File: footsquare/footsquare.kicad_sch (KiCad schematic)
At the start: 6 parts, among them J1 USB_B, U1 Trill_Craft, U2 Teensy-LC

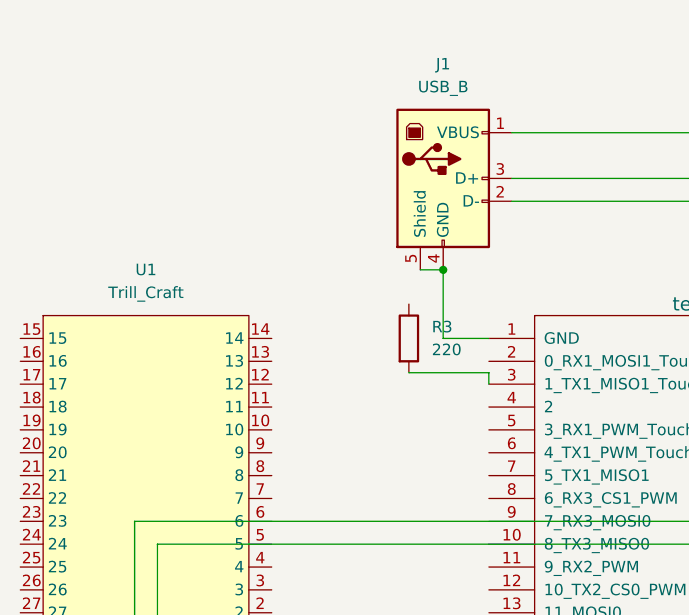
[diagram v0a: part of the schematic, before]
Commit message: new version with encoder and ground plane
-ground plane added
-encoder added
-outline added
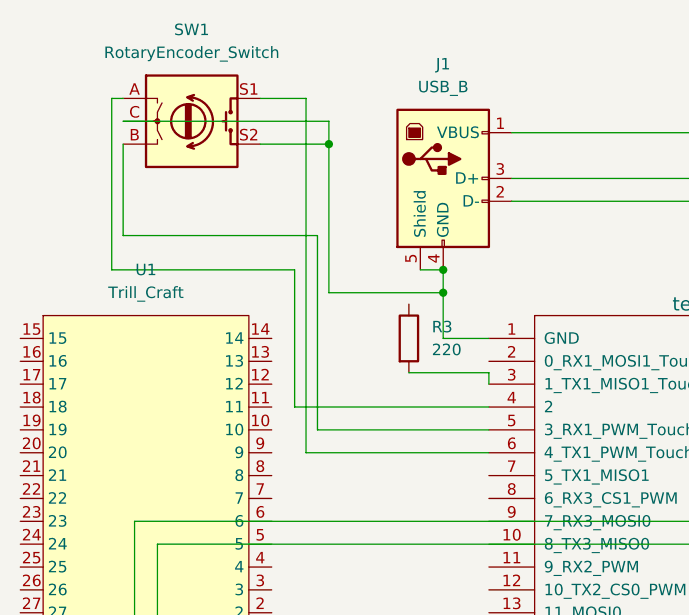
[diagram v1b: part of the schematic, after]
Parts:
- added SW1: RotaryEncoder_Switch, Rotary_Encoder:RotaryEncoder_Alps_EC11E-Switch_Vertical_H20mm, symbol Device:RotaryEncoder_Switch
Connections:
- net at J1.4 (GND), J1.5 (Shield), U2.1 (GND): now also SW1.C, SW1.S2
- net at U2.4 (2): now also SW1.A
- net at U2.5 (3_RX1_PWM_Touch): now also SW1.B
- net at U2.6 (4_TX1_PWM_Touch): now also SW1.S1
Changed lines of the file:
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@@
 (kicad_sch (version 20211123) (generator eeschema)
   (paper "A4")
+  (junction (at 204.47 62.23) (diameter 0) (color 0 0 0 0)
+  )
   (junction (at 274.32 90.17) (diameter 0) (color 0 0 0 0)
   )
+  (junction (at 191.77 45.72) (diameter 0) (color 0 0 0 0)
+  )
   (junction (at 269.24 105.41) (diameter 0) (color 0 0 0 0)
   )
@@
   (junction (at 271.78 105.41) (diameter 0) (color 0 0 0 0)
   )
+  (wire (pts (xy 187.96 59.69) (xy 187.96 74.93))
+    (stroke (width 0) (type default) (color 0 0 0 0))
+  )
   (wire (pts (xy 281.94 105.41) (xy 281.94 99.06))
     (stroke (width 0) (type default) (color 0 0 0 0))
@@
     (stroke (width 0) (type default) (color 0 0 0 0))
   )
+  (wire (pts (xy 187.96 74.93) (xy 209.55 74.93))
+    (stroke (width 0) (type default) (color 0 0 0 0))
+  )
   (wire (pts (xy 269.24 82.55) (xy 274.32 82.55))
     (stroke (width 0) (type default) (color 0 0 0 0))
@@
     (stroke (width 0) (type default) (color 0 0 0 0))
   )
+  (wire (pts (xy 168.91 43.18) (xy 191.77 43.18))
+    (stroke (width 0) (type default) (color 0 0 0 0))
+  )
   (wire (pts (xy 175.26 129.54) (xy 271.78 129.54))
     (stroke (width 0) (type default) (color 0 0 0 0))
@@
     (stroke (width 0) (type default) (color 0 0 0 0))
   )
+  (wire (pts (xy 168.91 55.88) (xy 190.5 55.88))
+    (stroke (width 0) (type default) (color 0 0 0 0))
+  )
   (wire (pts (xy 201.93 59.69) (xy 204.47 59.69))
     (stroke (width 0) (type default) (color 0 0 0 0))
   )
-  (wire (pts (xy 204.47 67.31) (xy 204.47 59.69))
+  (wire (pts (xy 167.64 59.69) (xy 187.96 59.69))
+    (stroke (width 0) (type default) (color 0 0 0 0))
+  )
+  (wire (pts (xy 190.5 55.88) (xy 190.5 77.47))
+    (stroke (width 0) (type default) (color 0 0 0 0))
+  )
+  (wire (pts (xy 204.47 67.31) (xy 204.47 62.23))
+    (stroke (width 0) (type default) (color 0 0 0 0))
+  )
+  (wire (pts (xy 168.91 40.64) (xy 167.64 40.64))
     (stroke (width 0) (type default) (color 0 0 0 0))
   )
@@
     (stroke (width 0) (type default) (color 0 0 0 0))
   )
+  (wire (pts (xy 191.77 43.18) (xy 191.77 45.72))
+    (stroke (width 0) (type default) (color 0 0 0 0))
+  )
   (wire (pts (xy 172.72 90.17) (xy 269.24 90.17))
     (stroke (width 0) (type default) (color 0 0 0 0))
   )
+  (wire (pts (xy 191.77 62.23) (xy 204.47 62.23))
+    (stroke (width 0) (type default) (color 0 0 0 0))
+  )
   (wire (pts (xy 200.66 71.12) (xy 209.55 71.12))
     (stroke (width 0) (type default) (color 0 0 0 0))
@@
     (stroke (width 0) (type default) (color 0 0 0 0))
   )
+  (wire (pts (xy 168.91 45.72) (xy 168.91 55.88))
+    (stroke (width 0) (type default) (color 0 0 0 0))
+  )
+  (wire (pts (xy 189.23 80.01) (xy 209.55 80.01))
+    (stroke (width 0) (type default) (color 0 0 0 0))
+  )
   (wire (pts (xy 172.72 90.17) (xy 172.72 113.03))
     (stroke (width 0) (type default) (color 0 0 0 0))
   )
+  (wire (pts (xy 167.64 40.64) (xy 167.64 59.69))
+    (stroke (width 0) (type default) (color 0 0 0 0))
+  )
   (wire (pts (xy 271.78 105.41) (xy 281.94 105.41))
     (stroke (width 0) (type default) (color 0 0 0 0))
@@
     (stroke (width 0) (type default) (color 0 0 0 0))
   )
+  (wire (pts (xy 191.77 45.72) (xy 191.77 62.23))
+    (stroke (width 0) (type default) (color 0 0 0 0))
+  )
   (wire (pts (xy 274.32 44.45) (xy 212.09 44.45))
     (stroke (width 0) (type default) (color 0 0 0 0))
@@
     (stroke (width 0) (type default) (color 0 0 0 0))
   )
+  (wire (pts (xy 184.15 45.72) (xy 191.77 45.72))
+    (stroke (width 0) (type default) (color 0 0 0 0))
+  )
+  (wire (pts (xy 204.47 62.23) (xy 204.47 59.69))
+    (stroke (width 0) (type default) (color 0 0 0 0))
+  )
+  (wire (pts (xy 184.15 40.64) (xy 189.23 40.64))
+    (stroke (width 0) (type default) (color 0 0 0 0))
+  )
   (wire (pts (xy 209.55 71.12) (xy 209.55 72.39))
     (stroke (width 0) (type default) (color 0 0 0 0))
   )
+  (wire (pts (xy 190.5 77.47) (xy 209.55 77.47))
+    (stroke (width 0) (type default) (color 0 0 0 0))
+  )
   (wire (pts (xy 271.78 69.85) (xy 271.78 49.53))
+    (stroke (width 0) (type default) (color 0 0 0 0))
+  )
+  (wire (pts (xy 189.23 40.64) (xy 189.23 80.01))
     (stroke (width 0) (type default) (color 0 0 0 0))
   )
@@
     (pin "2")
   )
+  (symbol (lib_id "Device:RotaryEncoder_Switch") (at 176.53 43.18 0) (unit 1)
+    (in_bom yes) (on_board yes) (fields_autoplaced)
+    (property "Reference" "SW1" (id 0) (at 176.53 33.02 0))
+    (property "Value" "RotaryEncoder_Switch" (id 1) (at 176.53 35.56 0))
+    (property "Footprint" "Rotary_Encoder:RotaryEncoder_Alps_EC11E-Switch_Vertical_H20mm" (id 2) (at 172.72 39.116 0)
+      (effects (font (size 1.27 1.27)) hide)
+    )
+    (property "Datasheet" "~" (id 3) (at 176.53 36.576 0)
+      (effects (font (size 1.27 1.27)) hide)
+    )
+    (pin "A")
+    (pin "B")
+    (pin "C")
+    (pin "S1")
+    (pin "S2")
+  )
   (sheet_instances
     (path "/" (page "1"))
@@
       (reference "R3") (unit 1) (value "220") (footprint "Resistor_THT:R_Axial_DIN0204_L3.6mm_D1.6mm_P7.62mm_Horizontal")
     )
+    (path "/dffaa8cf-9954-4be7-9249-735cc6841ad0"
+      (reference "SW1") (unit 1) (value "RotaryEncoder_Switch") (footprint "Rotary_Encoder:RotaryEncoder_Alps_EC11E-Switch_Vertical_H20mm")
+    )
     (path "/122f87b5-23fc-405d-ba50-50cf130fb212"
